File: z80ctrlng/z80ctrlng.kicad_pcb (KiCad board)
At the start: 4 copper layers, 101.6 x 53.3 mm, 67 parts, among them J1 RCBUS, J11 U254-051T-4BH81-S2S, J3 UDPI, J5 XKTF-0803-0, J6 UEXT, J9 SM04B-SRSS-TB, Q3 BSS138, SW1 RESET, SW2 BANK_EN, SW4 PROG_EN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

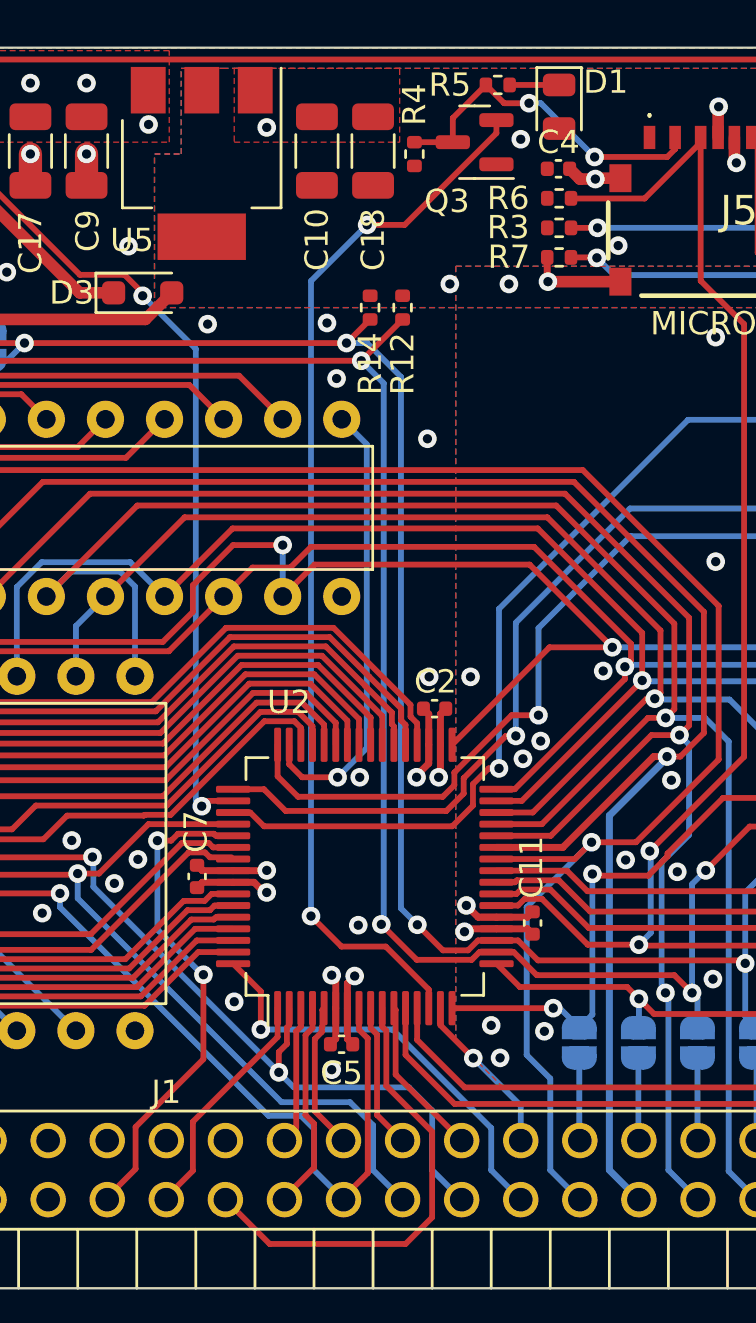
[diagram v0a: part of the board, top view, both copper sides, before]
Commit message: Updating silkscreen
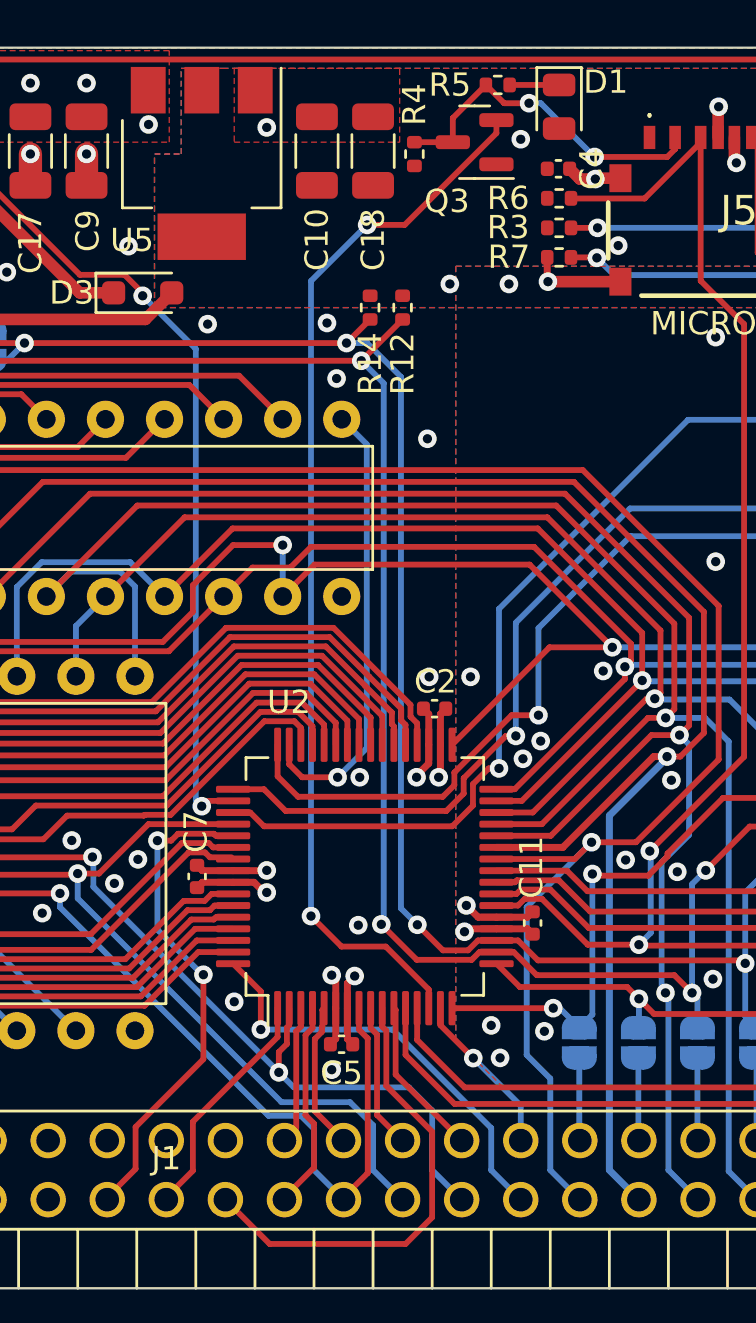
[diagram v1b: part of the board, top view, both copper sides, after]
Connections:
- net PB4 renamed TXB
- net PB5 renamed RXB
- net PF4 renamed TXF
- net PF5 renamed RXF
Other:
- board text removed: "PB4"
- board text removed: "PB5"

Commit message: Misc tweaks to boards
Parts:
- moved R2 1.44 mm to (215.8, 87.5)
- moved D4 1.42 mm to (216.5, 86.0)
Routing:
- net +3.3V: track 67.4 -> 116.6 mm, vias 14 -> 7
- net TXC: track 33.9 -> 48.7 mm, vias 2 -> 1
- net SCK: track 73.2 -> 78.3 mm, vias 6 -> 5
- net RXC: track 36.5 -> 40.6 mm, vias 2 -> 1
- net +5V: track 16.3 -> 19.5 mm, vias 34 -> 36
- net MOSI: track 75.8 -> 78.3 mm, vias 3 -> 2
- net SCL: track 128.5 -> 131.0 mm
- net GND: track 40.8 -> 38.4 mm, vias 90 -> 101
- net /D0: track 96.8 -> 99.0 mm
- net UPDI: track 64.2 -> 66.2 mm
- net ~{CS}: track 33.2 -> 34.6 mm
- net SDA: track 133.7 -> 135.1 mm
- net /D5: track 75.6 -> 76.4 mm
- net /D4: track 69.4 -> 68.6 mm
- net Net-(SW4A-C): track 7.84 -> 8.44 mm
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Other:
- board text added: "COMM"
- board text added: "PROG"
- board text added: "SERIAL CONFIG"
- board text added: "USB"
- board text removed: "USB PROG"

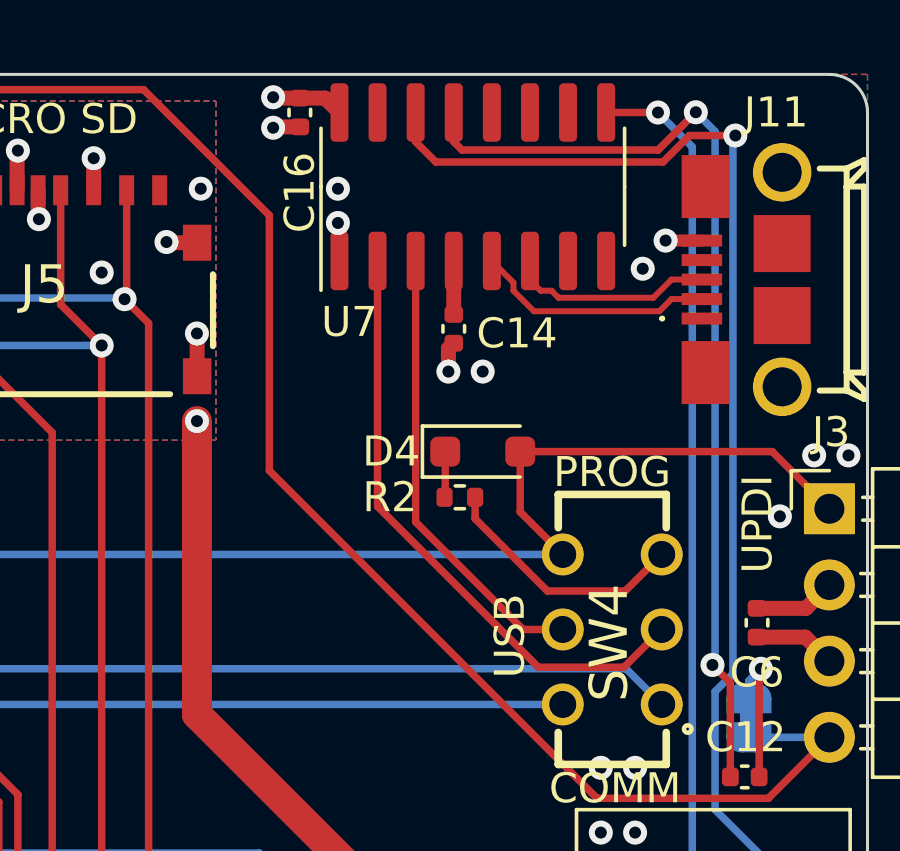
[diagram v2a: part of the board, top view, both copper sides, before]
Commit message: Put resistor before switch to avoid parasitic powering of the board
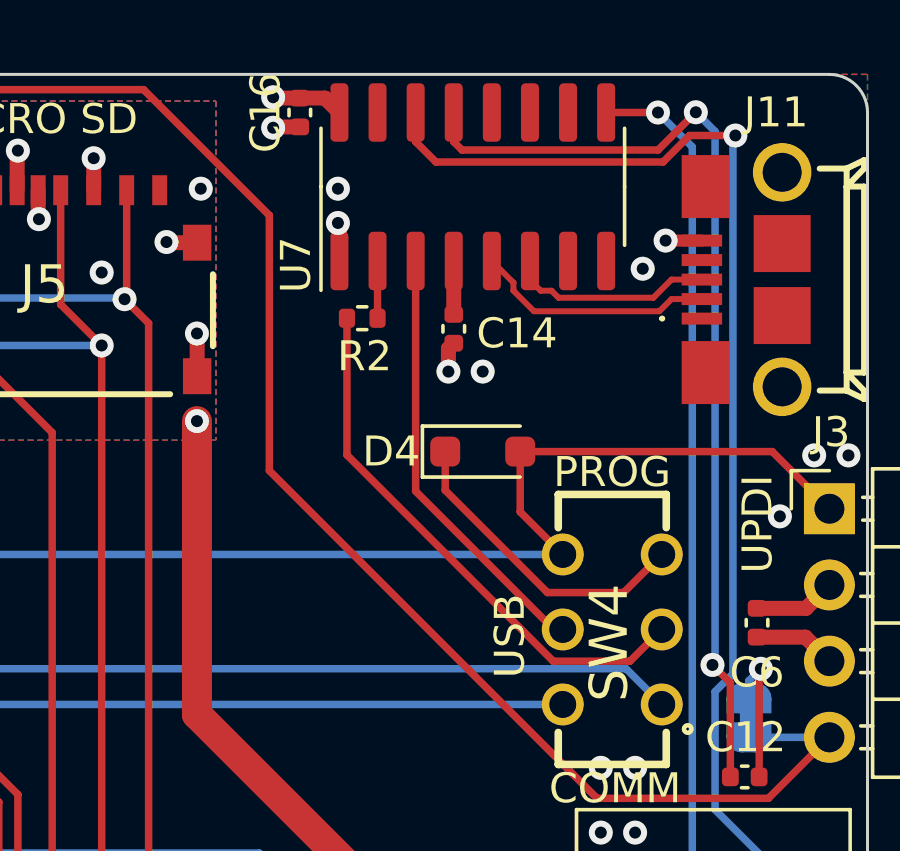
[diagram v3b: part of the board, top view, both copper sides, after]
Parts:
- R2: value 4.7K -> 1K
- moved R2 6.80 mm to (212.5, 81.5)
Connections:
- R2 pad 1: Net-(SW4A-C) -> Net-(U7-TXD)
- R2 pad 2: Net-(D4-K) -> /Peripherals/USBTX
- SW4 pad 3: Net-(SW4A-C) -> Net-(D4-K)
- U7 pad 2: /Peripherals/USBTX -> Net-(U7-TXD)
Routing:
- net Net-(D4-K): track 1.53 -> 10.4 mm
- net Net-(SW4A-C): track 8.44 -> 0.00 mm
- net /Peripherals/USBTX: track 20.4 -> 18.3 mm
- net Net-(U7-TXD): track 0.00 -> 1.91 mm
- net /Peripherals/USBRX: track 15.1 -> 14.5 mm
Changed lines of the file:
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@@
   (net 133 "TXB")
   (net 134 "/Peripherals/USBTX")
-  (net 135 "Net-(SW4A-C)")
+  (net 135 "Net-(U7-TXD)")
   (net 136 "Net-(U7-V3)")
   (net 137 "/USER6")
@@
     (property "ki_keywords" "USB UART Serial Converter Interface")
     (attr smd)
-    (fp_text reference "U7" (at -4.51 -4.1148) (layer "F.SilkS")
+    (fp_text reference "U7" (at -2.605 -5.8928 270) (layer "F.SilkS")
         (effects (font (size 1 1) (thickness 0.15)))
     )
@@
       (net 38 "GND") (pinfunction "GND") (pintype "power_in"))
     (pad "2" smd roundrect (at -2.475 -3.175 90) (size 1.95 0.6) (layers "F.Cu" "F.Paste" "F.Mask") (roundrect_rratio 0.25)
-      (net 134 "/Peripherals/USBTX") (pinfunction "TXD") (pintype "output"))
+      (net 135 "Net-(U7-TXD)") (pinfunction "TXD") (pintype "output"))
     (pad "3" smd roundrect (at -2.475 -1.905 90) (size 1.95 0.6) (layers "F.Cu" "F.Paste" "F.Mask") (roundrect_rratio 0.25)
       (net 132 "/Peripherals/USBRX") (pinfunction "RXD") (pintype "input"))
@@
     (fp_arc (start 4.02 5.42) (mid 4.121556 5.533647) (end 4.22 5.65)
       (stroke (width 0.05) (type solid)) (layer "F.CrtYd"))
-    (fp_arc (start 5.3 6.1) (mid 4.714381 5.984481) (end 4.22 5.65)
+    (fp_arc (start 5.3 6.1) (mid 4.714387 5.984475) (end 4.22 5.65)
       (stroke (width 0.05) (type solid)) (layer "F.CrtYd"))
     (fp_arc (start 7.25 -1.94) (mid 8.650198 0.005) (end 7.25 1.95)
       (stroke (width 0.05) (type solid)) (layer "F.CrtYd"))
-    (fp_arc (start 7.25 4.1) (mid 6.682004 5.496828) (end 5.3 6.1)
+    (fp_arc (start 7.25 4.1) (mid 6.682004 5.496829) (end 5.3 6.1)
       (stroke (width 0.05) (type solid)) (layer "F.CrtYd"))
     (fp_line (start -6.6 -3.4) (end -6.6 4.05)
@@
     (fp_arc (start 5.378013 5.447558) (mid 4.942442 5.378013) (end 4.6 5.1)
       (stroke (width 0.1) (type solid)) (layer "F.Fab"))
-    (fp_arc (start 6.6 4.1) (mid 6.222443 5.037354) (end 5.3 5.45)
+    (fp_arc (start 6.6 4.1) (mid 6.222442 5.03735) (end 5.3 5.45)
       (stroke (width 0.1) (type solid)) (layer "F.Fab"))
     (pad "1" thru_hole circle (at -6.6 0 180) (size 3 3) (drill 1.9) (layers "*.Cu" "*.Mask")
@@
       (net 134 "/Peripherals/USBTX") (pinfunction "B") (pintype "passive"))
     (pad "3" thru_hole circle (at 2.5 1.65 90) (size 1.4 1.4) (drill 0.9) (layers "*.Cu" "*.Mask")
-      (net 135 "Net-(SW4A-C)") (pinfunction "C") (pintype "passive"))
+      (net 126 "Net-(D4-K)") (pinfunction "C") (pintype "passive"))
     (pad "4" thru_hole circle (at -2.5 -1.65 90) (size 1.4 1.4) (drill 0.9) (layers "*.Cu" "*.Mask")
       (net 142 "TXF") (pinfunction "A") (pintype "passive"))
@@
   )
   (footprint "Resistor_SMD:R_0402_1005Metric" (layer "F.Cu")
-    (at 215.773 87.503 180)
+    (at 212.5198 81.534 180)
     (descr "Resistor SMD 0402 (1005 Metric), square (rectangular) end terminal, IPC_7351 nominal, (Body size source: IPC-SM-782 page 72, https://www.pcb-3d.com/wordpress/wp-content/uploads/ipc-sm-782a_amendment_1_and_2.pdf), generated with kicad-footprint-generator")
     (tags "resistor")
@@
     (property "ki_keywords" "R resistor")
     (attr smd)
-    (fp_text reference "R2" (at 2.33 0) (layer "F.SilkS")
+    (fp_text reference "R2" (at -0.0782 -1.27) (layer "F.SilkS")
         (effects (font (size 1 1) (thickness 0.15)))
     )
-    (fp_text value "4.7K" (at 0 1.17) (layer "F.Fab")
+    (fp_text value "1K" (at 0 1.17) (layer "F.Fab")
         (effects (font (size 1 1) (thickness 0.15)))
     )
@@
       (stroke (width 0.1) (type solid)) (layer "F.Fab"))
     (pad "1" smd roundrect (at -0.51 0 180) (size 0.54 0.64) (layers "F.Cu" "F.Paste" "F.Mask") (roundrect_rratio 0.25)
-      (net 135 "Net-(SW4A-C)") (pintype "passive"))
+      (net 135 "Net-(U7-TXD)") (pintype "passive"))
     (pad "2" smd roundrect (at 0.51 0 180) (size 0.54 0.64) (layers "F.Cu" "F.Paste" "F.Mask") (roundrect_rratio 0.25)
-      (net 126 "Net-(D4-K)") (pintype "passive"))
+      (net 134 "/Peripherals/USBTX") (pintype "passive"))
     (model "${KICAD6_3DMODEL_DIR}/Resistor_SMD.3dshapes/R_0402_1005Metric.wrl"
       (offset (xyz 0 0 0))
@@
     (property "ki_keywords" "capacitor cap")
     (attr smd)
-    (fp_text reference "C16" (at 2.667 0 90) (layer "F.SilkS")
+    (fp_text reference "C16" (at 0 1.143 90) (layer "F.SilkS")
         (effects (font (size 1 1) (thickness 0.15)))
     )
@@
     (property "Sheetfile" "peripherals.kicad_sch")
     (property "Sheetname" "Peripherals")
+    (property "dnp" "")
     (property "ki_description" "Generic connector, single row, 01x04, script generated (kicad-library-utils/schlib/autogen/connector/)")
     (property "ki_keywords" "connector")
@@
   (via (at 165.1635 79.0575) (size 0.8) (drill 0.4) (layers "F.Cu" "B.Cu") (net 121))
   (via (at 164.846 81.407016) (size 0.8) (drill 0.4) (layers "F.Cu" "B.Cu") (net 121))
-  (segment (start 219.204 89.408) (end 217.785 87.989) (width 0.25) (layer "F.Cu") (net 122))
   (segment (start 190.4776 105.9912) (end 190.4776 105.070524) (width 0.25) (layer "F.Cu") (net 122))
-  (segment (start 217.785 87.989) (end 217.785 85.979) (width 0.25) (layer "F.Cu") (net 122))
   (segment (start 181.4953 106.8832) (end 189.5856 106.8832) (width 0.25) (layer "F.Cu") (net 122))
   (segment (start 180.1651 106.2905) (end 180.9026 106.2905) (width 0.25) (layer "F.Cu") (net 122))
   (segment (start 180.9026 106.2905) (end 181.4953 106.8832) (width 0.25) (layer "F.Cu") (net 122))
   (segment (start 189.5856 106.8832) (end 190.4776 105.9912) (width 0.25) (layer "F.Cu") (net 122))
+  (segment (start 217.785 87.989) (end 219.204 89.408) (width 0.25) (layer "F.Cu") (net 122))
   (segment (start 217.785 85.979) (end 226.187 85.979) (width 0.25) (layer "F.Cu") (net 122))
   (segment (start 191.154124 104.394) (end 191.595481 104.394) (width 0.25) (layer "F.Cu") (net 122))
   (segment (start 226.187 85.979) (end 228.092 87.884) (width 0.25) (layer "F.Cu") (net 122))
+  (segment (start 217.785 85.979) (end 217.785 87.989) (width 0.25) (layer "F.Cu") (net 122))
   (segment (start 190.4776 105.070524) (end 191.154124 104.394) (width 0.25) (layer "F.Cu") (net 122))
   (via (at 191.595481 104.394) (size 0.8) (drill 0.4) (layers "F.Cu" "B.Cu") (net 122))
@@
   (segment (start 215.676 115.54) (end 217.932 113.284) (width 0.25) (layer "B.Cu") (net 125))
   (segment (start 212.83 115.54) (end 212.83 108.48) (width 0.25) (layer "B.Cu") (net 125))
-  (segment (start 215.285 85.979) (end 215.285 87.481) (width 0.25) (layer "F.Cu") (net 126))
-  (segment (start 215.285 87.481) (end 215.263 87.503) (width 0.25) (layer "F.Cu") (net 126))
+  (segment (start 221.234 90.678) (end 222.504 89.408) (width 0.25) (layer "F.Cu") (net 126))
+  (segment (start 215.285 85.979) (end 215.285 87.269) (width 0.25) (layer "F.Cu") (net 126))
+  (segment (start 215.285 87.269) (end 218.694 90.678) (width 0.25) (layer "F.Cu") (net 126))
+  (segment (start 218.694 90.678) (end 221.234 90.678) (width 0.25) (layer "F.Cu") (net 126))
   (segment (start 222.5595 104.074) (end 221.5995 104.074) (width 0.25) (layer "B.Cu") (net 127))
   (segment (start 223.8595 105.374) (end 222.5595 104.074) (width 0.25) (layer "B.Cu") (net 127))
@@
   (via (at 223.484402 112.334) (size 0.8) (drill 0.4) (layers "F.Cu" "B.Cu") (net 131))
   (segment (start 225.4095 112.334) (end 223.484402 112.334) (width 0.25) (layer "B.Cu") (net 131))
-  (segment (start 217.881851 91.908) (end 219.204 91.908) (width 0.25) (layer "F.Cu") (net 132))
-  (segment (start 214.2998 88.325949) (end 217.881851 91.908) (width 0.25) (layer "F.Cu") (net 132))
-  (segment (start 214.2998 79.626) (end 214.2998 88.325949) (width 0.25) (layer "F.Cu") (net 132))
+  (segment (start 218.908 91.908) (end 219.204 91.908) (width 0.25) (layer "F.Cu") (net 132))
+  (segment (start 214.2998 87.2998) (end 218.908 91.908) (width 0.25) (layer "F.Cu") (net 132))
+  (segment (start 214.2998 79.626) (end 214.2998 87.2998) (width 0.25) (layer "F.Cu") (net 132))
   (segment (start 189.6872 118.8212) (end 187.5776 116.7116) (width 0.25) (layer "F.Cu") (net 133))
   (segment (start 218.3638 118.8212) (end 189.6872 118.8212) (width 0.25) (layer "F.Cu") (net 133))
@@
   (via (at 226.822 104.074) (size 0.8) (drill 0.4) (layers "F.Cu" "B.Cu") (net 133))
   (segment (start 226.822 104.074) (end 225.4095 104.074) (width 0.25) (layer "B.Cu") (net 133))
-  (segment (start 221.2448 93.1672) (end 222.504 91.908) (width 0.25) (layer "F.Cu") (net 134))
-  (segment (start 213.0298 79.626) (end 213.0298 87.8078) (width 0.25) (layer "F.Cu") (net 134))
-  (segment (start 218.3892 93.1672) (end 221.2448 93.1672) (width 0.25) (layer "F.Cu") (net 134))
-  (segment (start 213.0298 87.8078) (end 218.3892 93.1672) (width 0.25) (layer "F.Cu") (net 134))
-  (segment (start 216.283 87.503) (end 216.283 88.2162) (width 0.25) (layer "F.Cu") (net 135))
-  (segment (start 218.694 90.6272) (end 221.2848 90.6272) (width 0.25) (layer "F.Cu") (net 135))
-  (segment (start 216.283 88.2162) (end 218.694 90.6272) (width 0.25) (layer "F.Cu") (net 135))
-  (segment (start 221.2848 90.6272) (end 222.504 89.408) (width 0.25) (layer "F.Cu") (net 135))
+  (segment (start 218.882946 92.964) (end 221.448 92.964) (width 0.25) (layer "F.Cu") (net 134))
+  (segment (start 212.0098 86.090854) (end 218.882946 92.964) (width 0.25) (layer "F.Cu") (net 134))
+  (segment (start 221.448 92.964) (end 222.504 91.908) (width 0.25) (layer "F.Cu") (net 134))
+  (segment (start 212.0098 81.534) (end 212.0098 86.090854) (width 0.25) (layer "F.Cu") (net 134))
+  (segment (start 213.0298 79.626) (end 213.0298 81.534) (width 0.25) (layer "F.Cu") (net 135))
   (segment (start 215.5698 79.626) (end 215.5698 81.407) (width 0.5) (layer "F.Cu") (net 136))
   (segment (start 180.1651 105.2905) (end 181.4905 105.2905) (width 0.25) (layer "F.Cu") (net 139))
